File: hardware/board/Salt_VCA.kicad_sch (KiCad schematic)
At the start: 40 parts

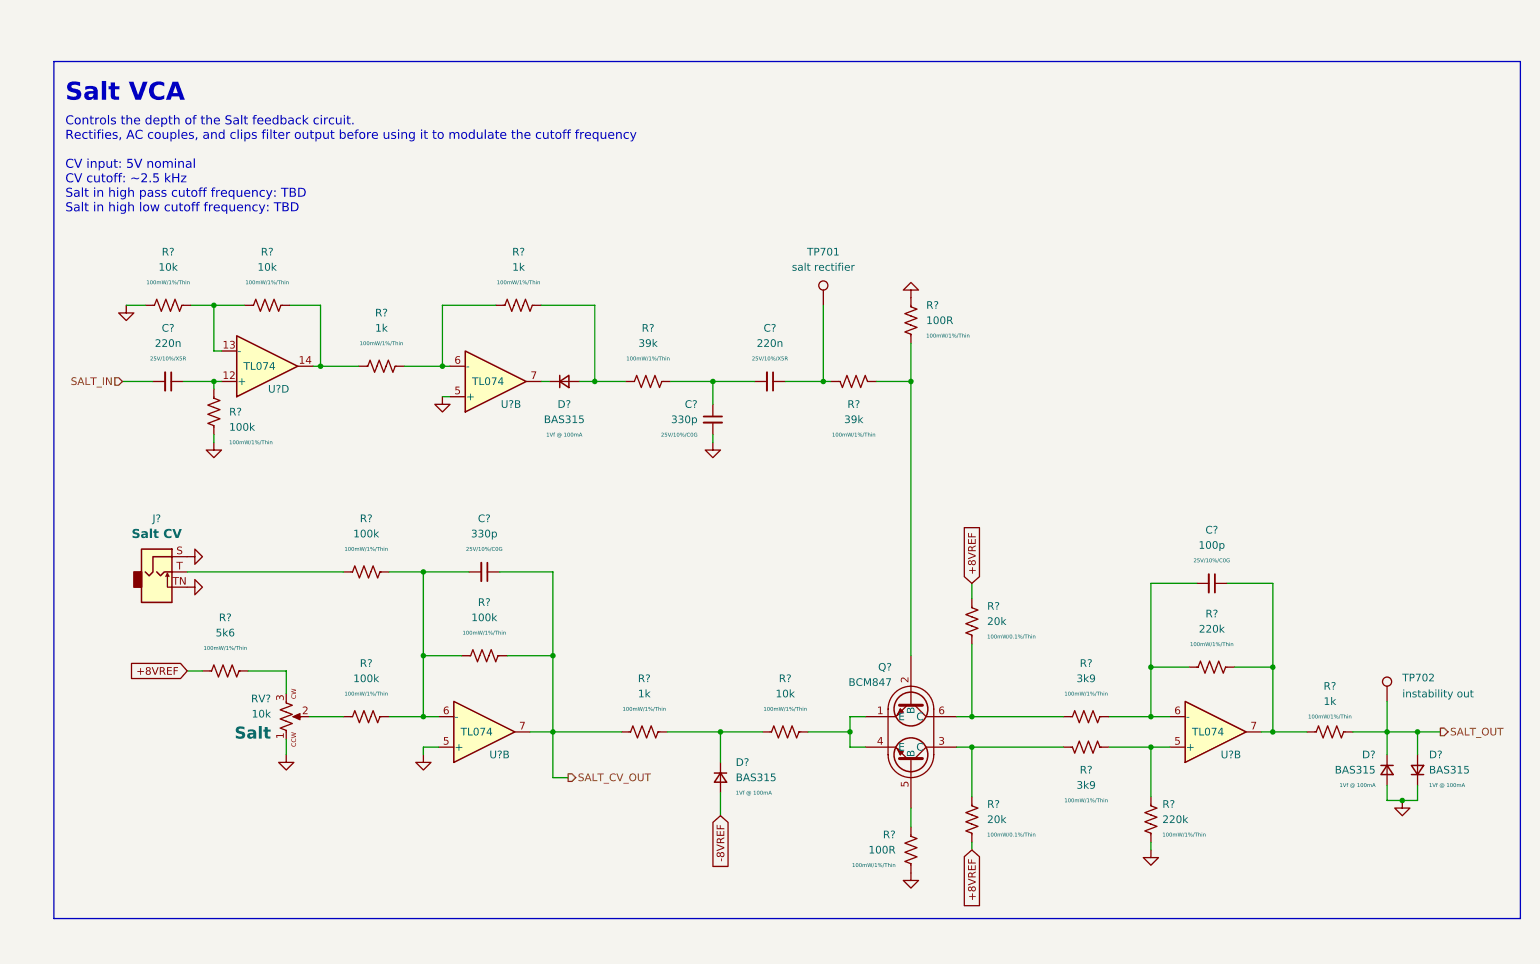
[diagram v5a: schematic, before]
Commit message: hardware: use new Winterbloom sheet layout
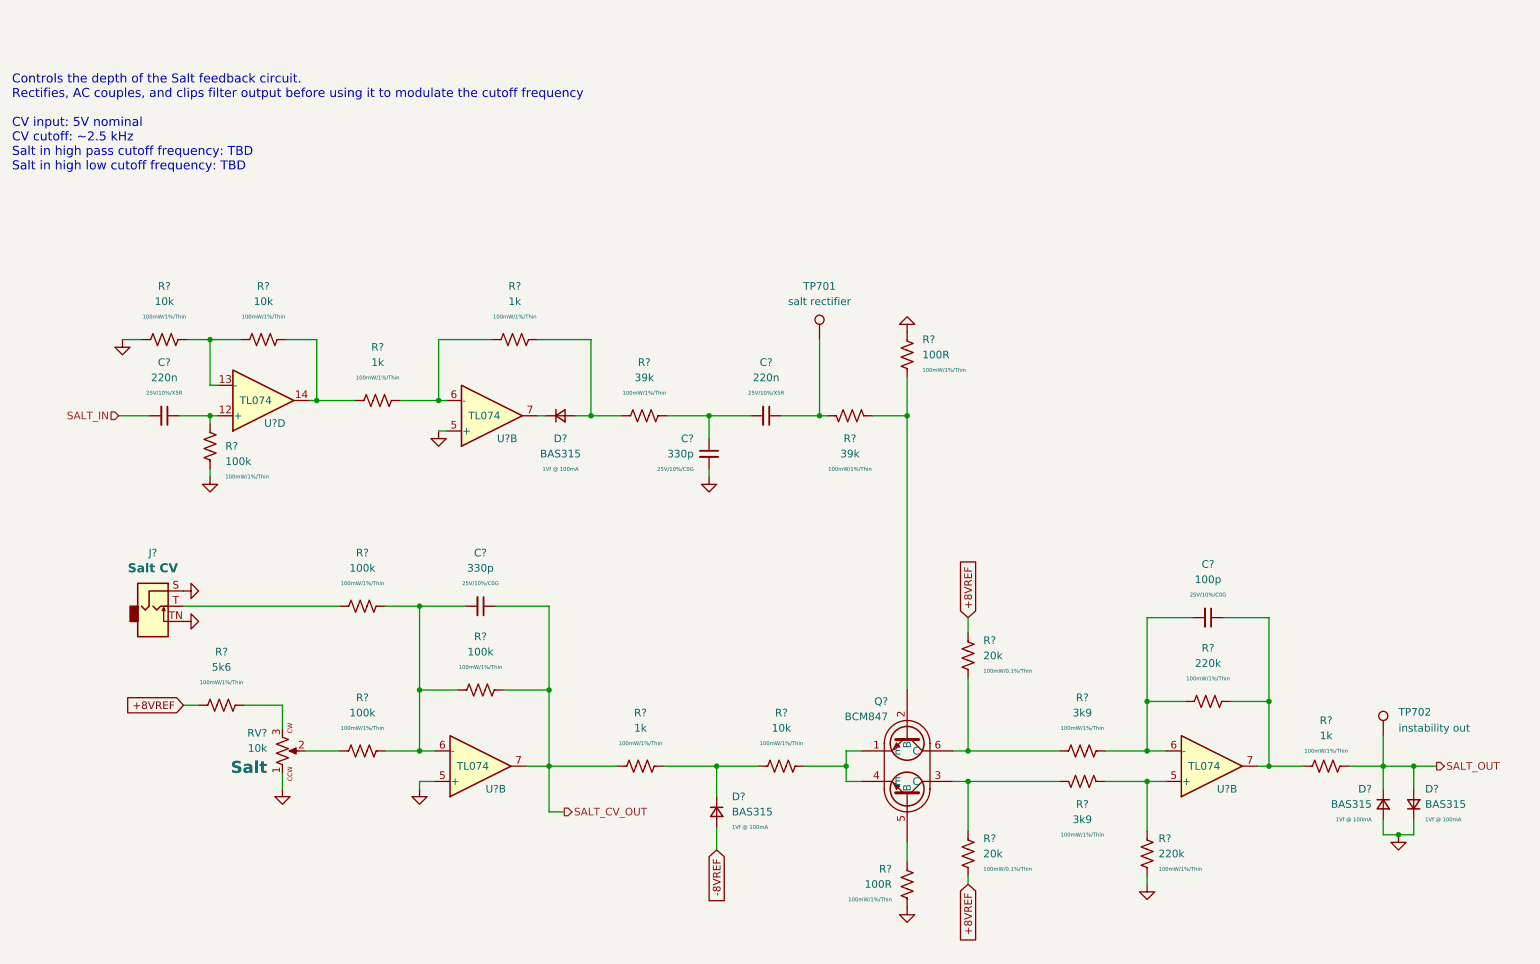
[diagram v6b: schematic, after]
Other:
- note removed: "Salt VCA"
- moved on the sheet: C?, D?, J?, Q?, R?, RV?, TP701, TP702, U?B, U?D

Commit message: hardware: finalize v3
- Updated version number and release date
- Swapped TL074C to TL074H
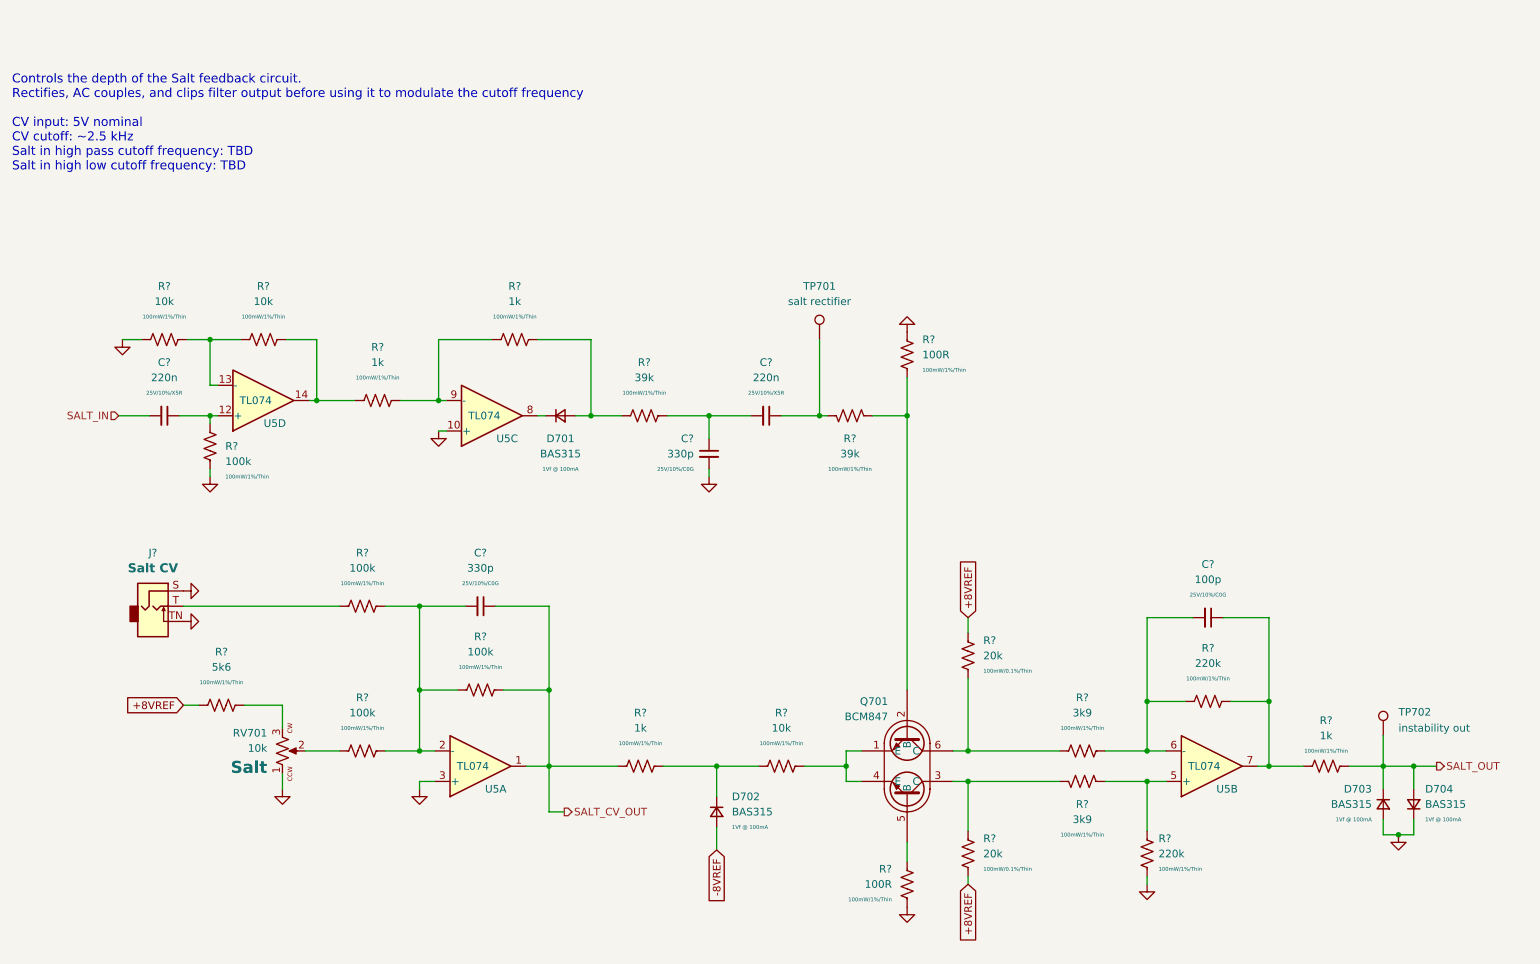
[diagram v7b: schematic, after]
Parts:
- U5: renamed from U?; DigiKey 296-7198-1-ND -> 296-TL074HIPWRCT-ND; LCSC C96507 -> C4370424; MPN TL074CPWR -> TL074HIPWR; Notes (none) -> TL074H over TL074C due to better input offset voltage
- gave numbers to parts that had none: 6
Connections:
- net GND: now also U5.10 (+), U5.3 (+); no longer U5.5 (+), U5.5 (+)
- net SALT_CV_OUT: now also U5.1; no longer U5.7
- net at C?.2, R?.1, R?.1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: now also U5.2 (-); no longer U5.6 (-)
- net at R?.1, R?.2: now also U5.9 (-); no longer U5.6 (-)
- net at D701.1 (K): now also U5.8; no longer U5.7
